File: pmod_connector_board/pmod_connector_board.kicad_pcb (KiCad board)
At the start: 4 copper layers, 120 x 10 mm, 4 parts, among them J10 Conn_02x06_Top_Bottom, J9 Conn_02x06_Top_Bottom, P1 Conn_02x06_Top_Bottom, P2 Conn_02x06_Top_Bottom

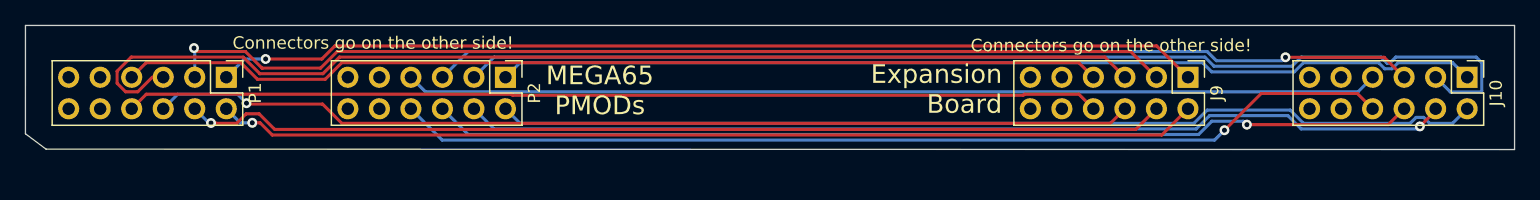
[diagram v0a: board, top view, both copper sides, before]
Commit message: correct PMOD placement on connector PCB
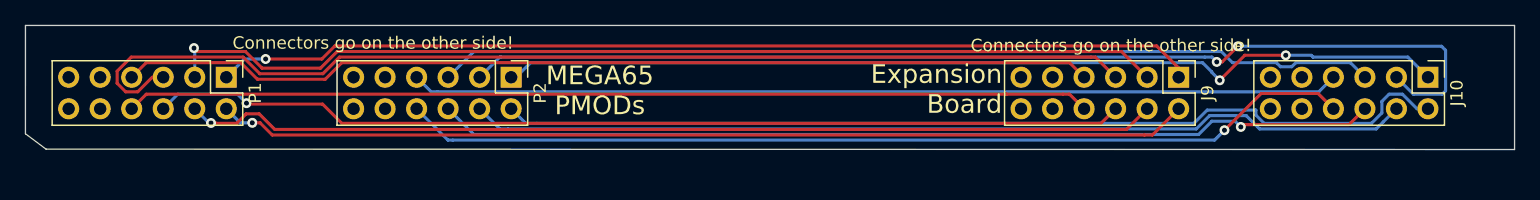
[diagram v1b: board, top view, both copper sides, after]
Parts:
- moved J10 3.16 mm to (133.0, 27.2)
- moved J9 0.75 mm to (112.9, 27.2)
- moved P2 0.46 mm to (59.1, 27.2)
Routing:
- net Net-(J10-Pad8): track 79.8 -> 76.1 mm, vias 1 -> 0
- net Net-(J10-Pad4): track 78.5 -> 74.9 mm
- net Net-(J10-Pad10): track 80.6 -> 77.0 mm
- net Net-(J10-Pad3): track 79.4 -> 75.9 mm, vias 1 -> 0
- net Net-(J10-Pad9): track 79.4 -> 76.0 mm
- net Net-(J10-Pad1): track 79.5 -> 76.5 mm, vias 0 -> 2
- net Net-(J10-Pad2): track 89.6 -> 87.2 mm, vias 0 -> 2
- net Net-(J10-Pad7): track 79.8 -> 77.5 mm
- net Net-(J9-Pad10): track 78.5 -> 77.7 mm
- net Net-(J9-Pad9): track 79.4 -> 78.7 mm
- net Net-(J9-Pad8): track 79.5 -> 78.8 mm
- net Net-(J9-Pad7): track 79.3 -> 78.5 mm
- net Net-(J9-Pad4): track 79.6 -> 78.8 mm
- net Net-(J9-Pad3): track 88.9 -> 88.2 mm
- net Net-(J9-Pad2): track 82.0 -> 81.3 mm

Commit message: reduce connector board to 2-layer for faster fabrication
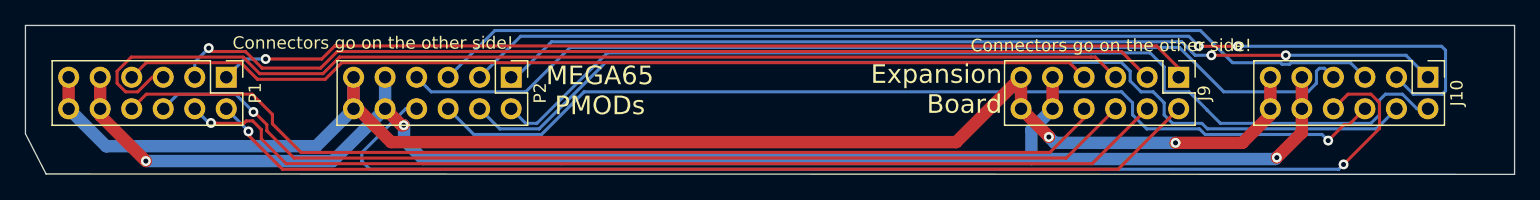
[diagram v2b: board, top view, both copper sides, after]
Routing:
- net GND: track 0.00 -> 120.7 mm, vias 0 -> 3
- net +3V3: track 0.00 -> 117.7 mm, vias 0 -> 2
- net Net-(J10-Pad10): track 77.0 -> 96.8 mm
- net Net-(J10-Pad7): track 77.5 -> 82.5 mm
- net Net-(J10-Pad8): track 76.1 -> 80.7 mm
- net Net-(J10-Pad4): track 74.9 -> 79.0 mm
- net Net-(J9-Pad10): track 77.7 -> 81.5 mm
- net Net-(J10-Pad9): track 76.0 -> 79.4 mm
- net Net-(J9-Pad9): track 78.7 -> 81.3 mm
- net Net-(J9-Pad7): track 78.5 -> 81.0 mm
- net Net-(J9-Pad8): track 78.8 -> 81.0 mm
- net Net-(J10-Pad3): track 75.9 -> 77.1 mm
- net Net-(J9-Pad2): track 81.3 -> 80.5 mm
- removed copper zone on In1.Cu, net +3V3
- removed copper zone on In2.Cu, net GND
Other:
- board size 120 x 10 mm -> 120 x 12 mm
- copper layers 4 -> 2
- board text added: "MEGA65 Expansion Board PMOD Bridge, revD.2 (C) Paul Gardner-Stephen 2024, CC-BY 4.0"
- board text removed: "MEGA65 Expansion Board PMOD Bridge, revA (C) Paul Gardner-Stephen 2024, CC-BY 4.0"
